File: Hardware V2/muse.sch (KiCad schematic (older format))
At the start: 47 parts, among them P1 3.5mm_line, P2 3.5mm_line, P3 RCA, P4 RCA, P5 ATX_PWR_OK, P6 ATX_PWR, P7 ATX_GND, P8 ATX_PS_ON, P9 LED_Signal, Q1 FQP30N06L, Q2 FQP30N06L, Q3 FQP30N06L, Q4 FQP30N06L, Q5 FQP30N06L, Q6 FQP30N06L, SW1 PWR_SW, U1 MSGEQ7, U2 MSGEQ7, U3 74LS595, U4 Spark_Core

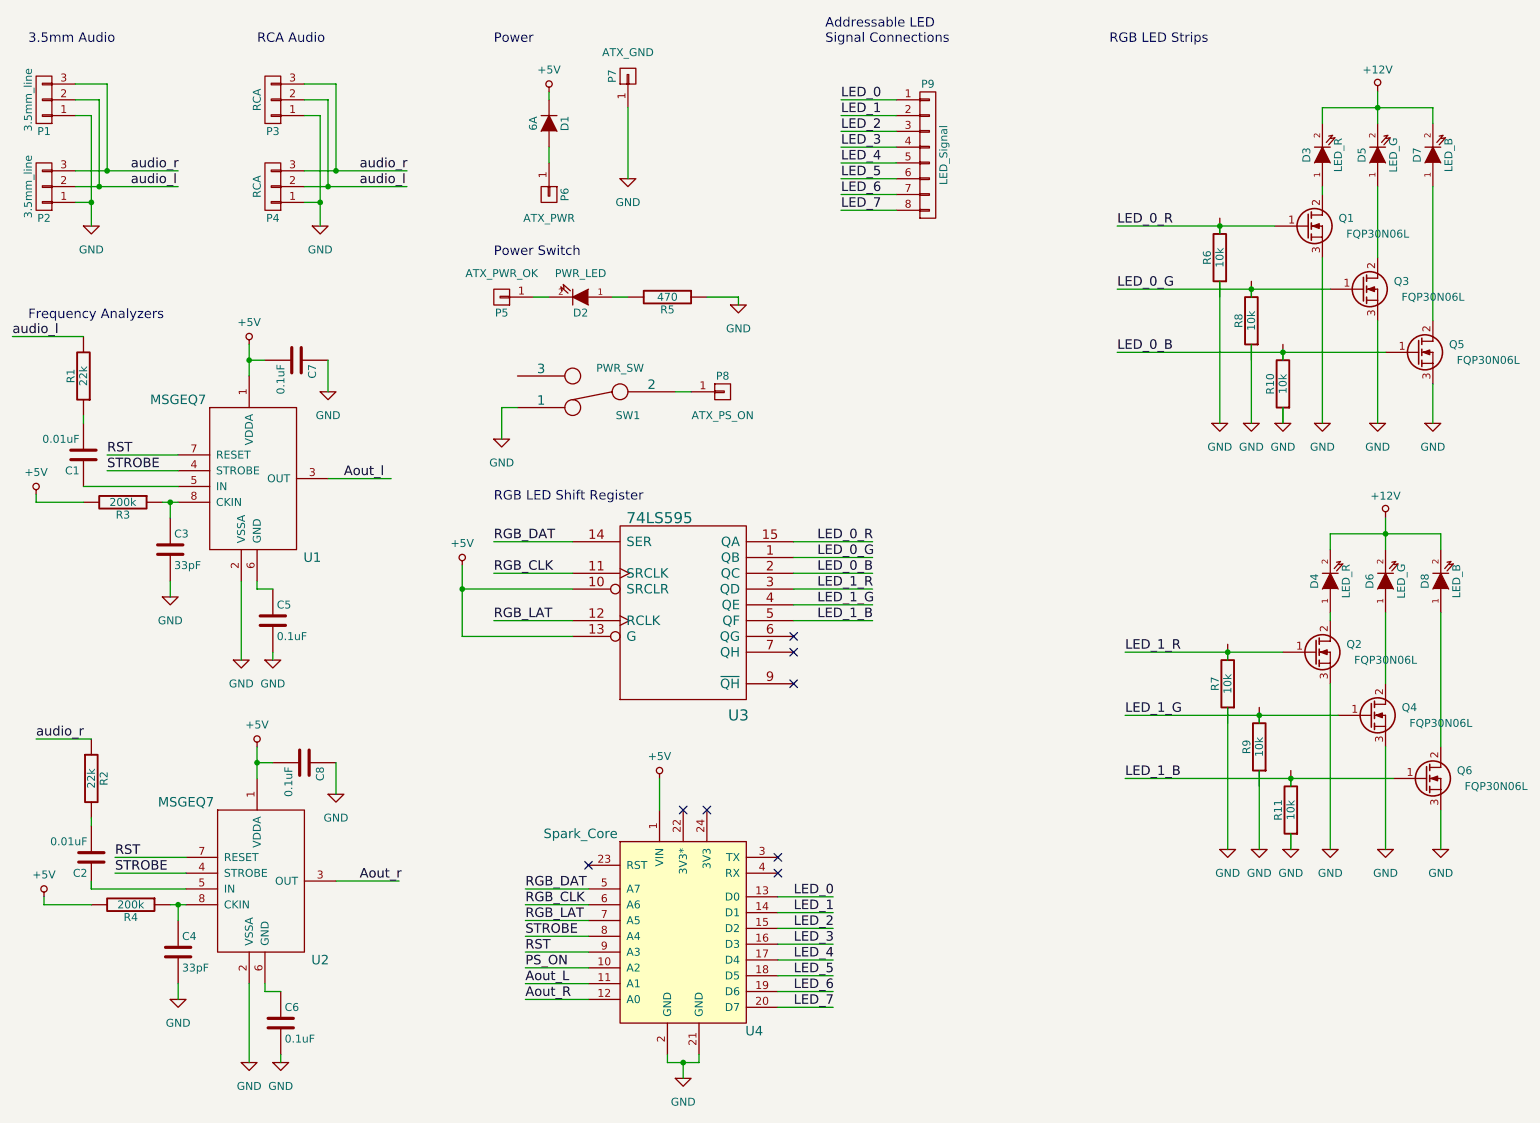
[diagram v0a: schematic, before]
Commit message: Finished updates schematic, removed gerber files
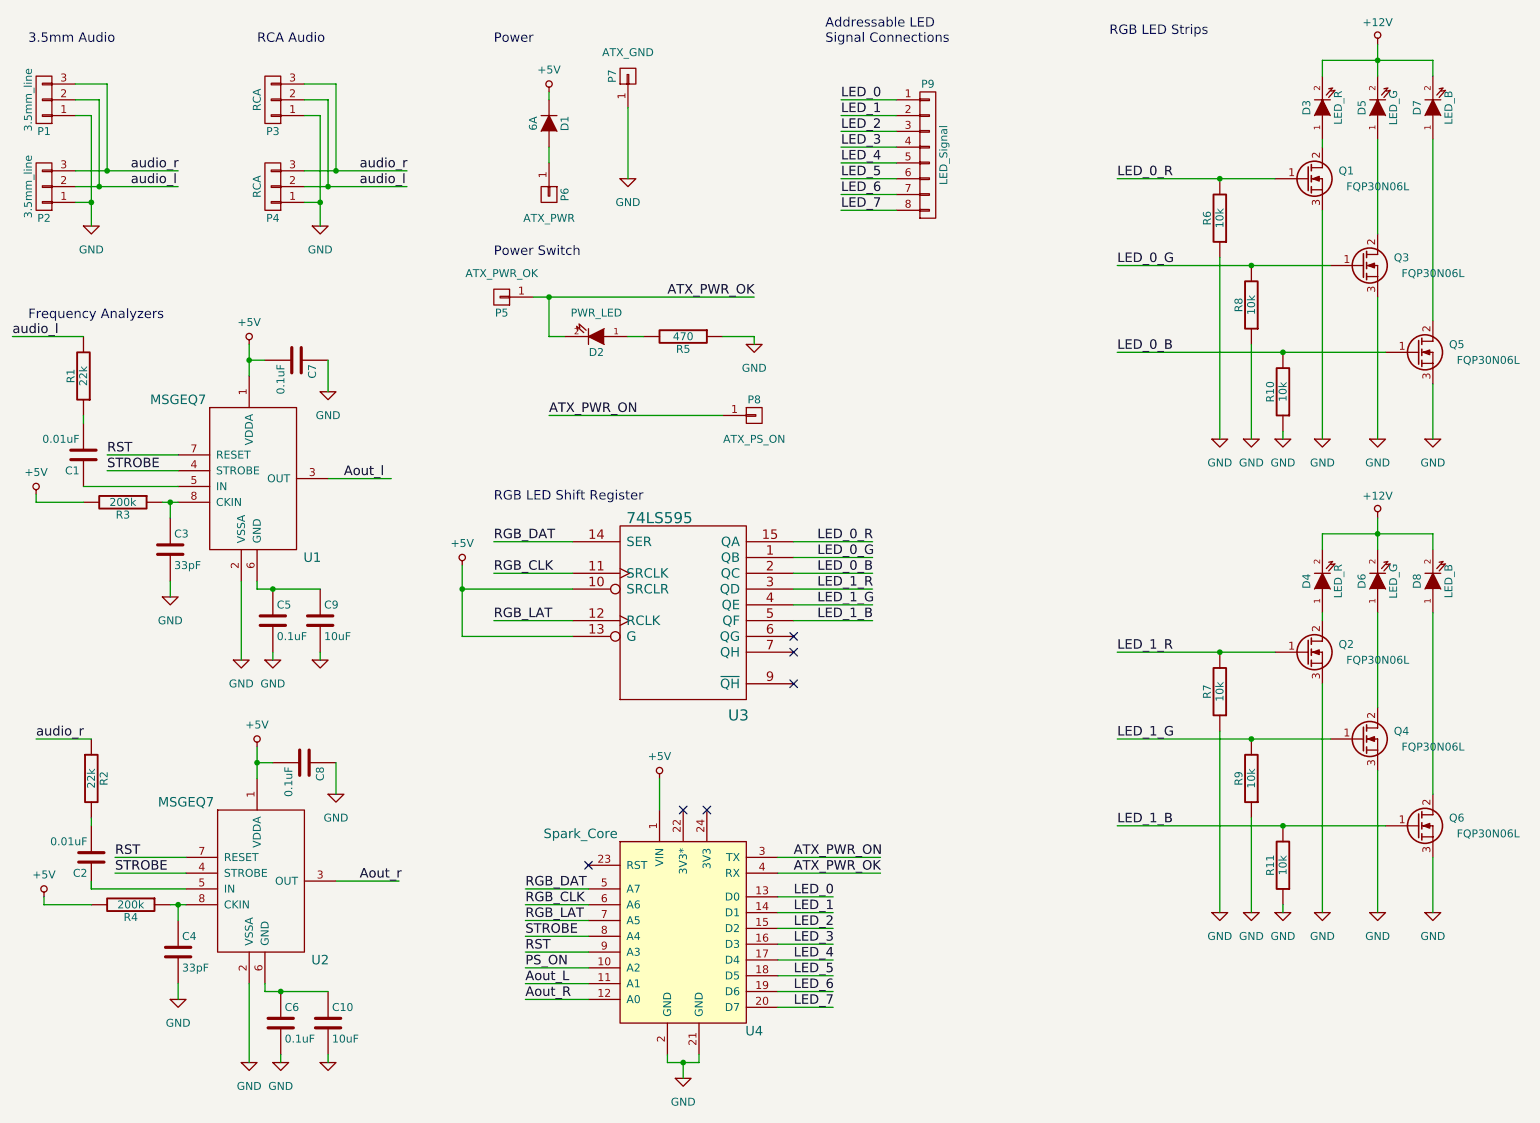
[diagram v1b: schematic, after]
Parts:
- removed SW1: PWR_SW, Pin_Headers:Pin_Header_Straight_1x02, symbol SWITCH_INV
- added C10, C9: 10uF, Capacitors_ThroughHole:C_Rect_L7_W2_P5, symbol C
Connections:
- net labels added: ATX_PWR_OK, ATX_PWR_ON
- wire segments 167 -> 143
- no-connect marks 8 -> 6
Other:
- moved on the sheet: D2, D3, D4, D5, D6, D7, D8, P8, Q1, Q2, Q3, Q4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

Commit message: Rev 2.0 Complete
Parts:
- removed D1: 6A, Diodes_ThroughHole:Diode_DO-41_SOD81_Horizontal_RM10, symbol D
- Q1, Q2, Q3, Q4, Q5, Q6: footprint Transistors_TO-220:TO-220_Neutral123_Vertical_LargePads -> TO_SOT_Packages_THT:TO-220_Neutral123_Vertical_LargePads
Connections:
- wire segments 143 -> 141
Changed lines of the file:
@@
 F 0 "Q3" H 9800 2200 50  0000 R CNN
 F 1 "FQP30N06L" H 10150 2100 50  0000 R CNN
-F 2 "Transistors_TO-220:TO-220_Neutral123_Vertical_LargePads" H 9700 2250 29  0001 C CNN
+F 2 "TO_SOT_Packages_THT:TO-220_Neutral123_Vertical_LargePads" H 9700 2250 29  0001 C CNN
 F 3 "" H 9500 2150 60  0000 C CNN
 	1    9500 2150
@@
 F 0 "Q1" H 9450 1650 50  0000 R CNN
 F 1 "FQP30N06L" H 9800 1550 50  0000 R CNN
-F 2 "Transistors_TO-220:TO-220_Neutral123_Vertical_LargePads" H 9350 1700 29  0001 C CNN
+F 2 "TO_SOT_Packages_THT:TO-220_Neutral123_Vertical_LargePads" H 9350 1700 29  0001 C CNN
 F 3 "" H 9150 1600 60  0000 C CNN
 	1    9150 1600
@@
 F 0 "Q5" H 10150 2750 50  0000 R CNN
 F 1 "FQP30N06L" H 10500 2650 50  0000 R CNN
-F 2 "Transistors_TO-220:TO-220_Neutral123_Vertical_LargePads" H 10050 2800 29  0001 C CNN
+F 2 "TO_SOT_Packages_THT:TO-220_Neutral123_Vertical_LargePads" H 10050 2800 29  0001 C CNN
 F 3 "" H 9850 2700 60  0000 C CNN
 	1    9850 2700
@@
 F 0 "Q4" H 9800 5200 50  0000 R CNN
 F 1 "FQP30N06L" H 10150 5100 50  0000 R CNN
-F 2 "Transistors_TO-220:TO-220_Neutral123_Vertical_LargePads" H 9700 5250 29  0001 C CNN
+F 2 "TO_SOT_Packages_THT:TO-220_Neutral123_Vertical_LargePads" H 9700 5250 29  0001 C CNN
 F 3 "" H 9500 5150 60  0000 C CNN
 	1    9500 5150
@@
 F 0 "Q2" H 9450 4650 50  0000 R CNN
 F 1 "FQP30N06L" H 9800 4550 50  0000 R CNN
-F 2 "Transistors_TO-220:TO-220_Neutral123_Vertical_LargePads" H 9350 4700 29  0001 C CNN
+F 2 "TO_SOT_Packages_THT:TO-220_Neutral123_Vertical_LargePads" H 9350 4700 29  0001 C CNN
 F 3 "" H 9150 4600 60  0000 C CNN
 	1    9150 4600
@@
 F 0 "Q6" H 10150 5750 50  0000 R CNN
 F 1 "FQP30N06L" H 10500 5650 50  0000 R CNN
-F 2 "Transistors_TO-220:TO-220_Neutral123_Vertical_LargePads" H 10050 5800 29  0001 C CNN
+F 2 "TO_SOT_Packages_THT:TO-220_Neutral123_Vertical_LargePads" H 10050 5800 29  0001 C CNN
 F 3 "" H 9850 5700 60  0000 C CNN
 	1    9850 5700
@@
 	1400 2600 950  2600
 Wire Wire Line
-	1450 6100 2050 6100
-Wire Wire Line
-	1450 6100 1450 6050
-Wire Wire Line
 	1450 5150 1100 5150
 Wire Wire Line
-	4350 1050 4350 1100
+	4350 1050 4350 1500
 $Comp
 L GND #PWR033
@@
 F 3 "" H 4650 2600 60  0000 C CNN
 	1    4650 2600
-	-1   0    0    1
+	1    0    0    -1
 $EndComp
 $Comp
@@
 $EndComp
 $Comp
-L D D1
-U 1 1 55FF8969
-P 4350 1250
-F 0 "D1" H 4350 1350 50  0000 C CNN
-F 1 "6A" H 4350 1150 50  0000 C CNN
-F 2 "Diodes_ThroughHole:Diode_DO-41_SOD81_Horizontal_RM10" H 4350 1250 60  0001 C CNN
-F 3 "" H 4350 1250 60  0000 C CNN
-	1    4350 1250
-	0    1    1    0
-$EndComp
-$Comp
 L CONN_01X01 P6
 U 1 1 5600CF8C
@@
 	0    1    1    0
 $EndComp
-Wire Wire Line
-	4350 1500 4350 1400
 $Comp
 L CONN_01X01 P7
@@
 Wire Wire Line
 	8800 5650 8800 6250
+Wire Wire Line
+	1450 6100 2050 6100
 $EndSCHEMATC
